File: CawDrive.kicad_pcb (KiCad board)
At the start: 4 copper layers, 60 x 60 mm, 112 parts, among them CN1 XT60PW-M, CN2 MR60PW-M, J1 Conn_01x04_Pin, J2 USB_B_Micro, Q1 IRF7480MTRPBF, Q2 IRF7480MTRPBF, Q3 IRF7480MTRPBF, Q4 IRF7480MTRPBF, Q5 IRF7480MTRPBF, Q6 IRF7480MTRPBF, SW1 B3U-1000P, U1 STM32F446RETx, U2 ISO1044BDR, U3 CH340K, U4 AMS1117-3.3, U5 DRV8323RSRGZR, Y1 16MHz

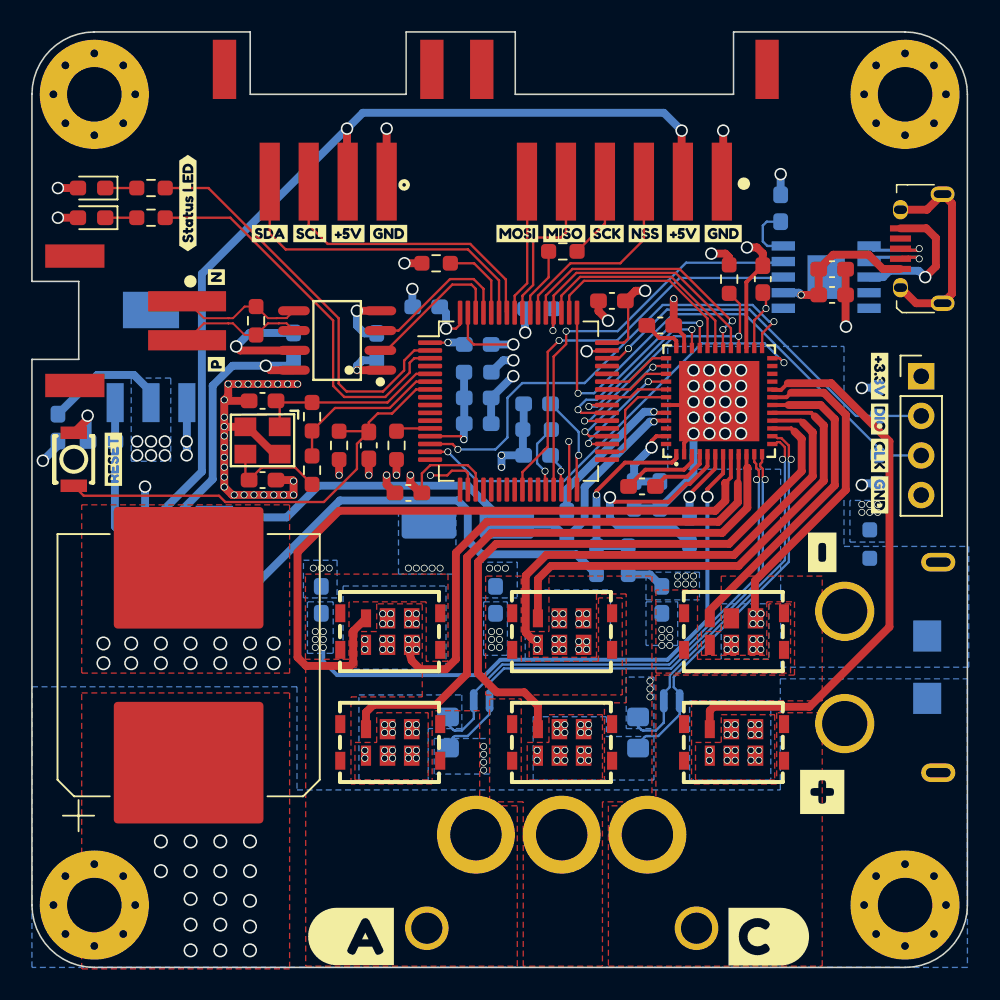
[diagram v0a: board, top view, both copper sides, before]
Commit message: 参考MIT驱动器进行改版
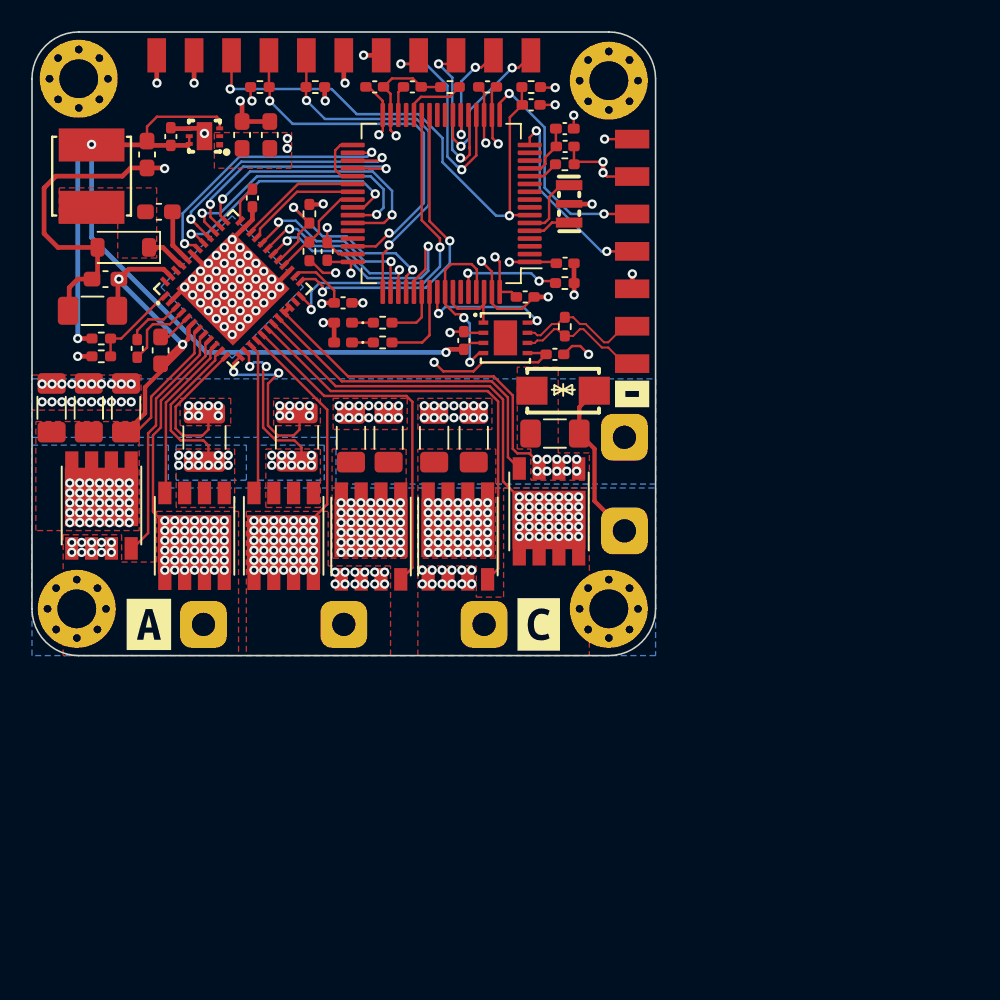
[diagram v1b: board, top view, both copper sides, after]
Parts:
- removed C10: 10uF, Capacitor_SMD:C_0603_1608Metric_Pad1.08x0.95mm_HandSolder
- removed C11, C13: 0.1uF, Capacitor_SMD:C_0603_1608Metric_Pad1.08x0.95mm_HandSolder
- removed C17, C19: 2.2uF/50V, Capacitor_SMD:C_0603_1608Metric_Pad1.08x0.95mm_HandSolder
- removed C18: 470uF/50V, Capacitor_SMD:CP_Elec_16x17.5
- removed CN1: XT60PW-M, Rick_Connector:XT60PW-M
- removed CN2: MR60PW-M, Rick_Connector:MR60PW-M
- removed FPC1: XH-6PWB, Rick_Connector:XH-6PWB
- removed FPC2: XH-4PWB, Rick_Connector:XH-4PWB
- removed FPC3: XH-2PWB, Rick_Connector:XH-2PWB
- removed the G*** at (167.5, 121.0)
- removed J2: USB_B_Micro, Rick_USB:Micro_USB_B_SMD
- removed NT1, NT2, NT3, NT4: NetTie_2, NetTie:NetTie-2_SMD_Pad0.5mm
- removed Q1, Q2, Q3, Q4, Q5, Q6: IRF7480MTRPBF, Rick_MOSFET:IRF7480MTRPBF
- removed R12: 510, Resistor_SMD:R_0603_1608Metric_Pad0.98x0.95mm_HandSolder
- removed R15: 1mΩ, Resistor_SMD:R_0805_2012Metric_Pad1.20x1.40mm_HandSolder
- removed R20: 10k, Resistor_SMD:R_0603_1608Metric_Pad0.98x0.95mm_HandSolder
- removed R4: 0, Resistor_SMD:R_0603_1608Metric_Pad0.98x0.95mm_HandSolder
- removed R7: 33, Resistor_SMD:R_0603_1608Metric_Pad0.98x0.95mm_HandSolder
- removed SW1: B3U-1000P, Rick_Switch:B3U-1000P
- removed U3: CH340K, Rick_Interface_USB:CH340K
- removed U4: AMS1117-3.3, Rick_Regulator_Linear:AMS1117-3.3
- removed Y1: 16MHz, Rick_Device:Crystal_16MHz_GND24
- removed kibuzzard-64D4C305: G***, kibuzzard-64D4C305
- removed kibuzzard-64D4C31F: G***, kibuzzard-64D4C31F
- removed kibuzzard-64D4C332: G***, kibuzzard-64D4C332
- removed kibuzzard-64D4C34A: G***, kibuzzard-64D4C34A
- removed kibuzzard-64D4C405: G***, kibuzzard-64D4C405
- removed kibuzzard-64D4C58A: G***, kibuzzard-64D4C58A
- removed kibuzzard-64D4C598: G***, kibuzzard-64D4C598
- removed kibuzzard-64D4C5A5: G***, kibuzzard-64D4C5A5
- removed kibuzzard-64D4C640: G***, kibuzzard-64D4C640
- removed kibuzzard-64D4C647: G***, kibuzzard-64D4C647
- removed kibuzzard-64D4C6F3: G***, kibuzzard-64D4C6F3
- removed kibuzzard-64D4C6FE: G***, kibuzzard-64D4C6FE
- removed kibuzzard-64D4C824: G***, kibuzzard-64D4C824
- removed kibuzzard-64D4C87F: G***, kibuzzard-64D4C87F
- removed kibuzzard-64D4C8BC: G***, kibuzzard-64D4C8BC
- removed kibuzzard-64D4C8D7: G***, kibuzzard-64D4C8D7
- removed kibuzzard-64D4C8F8: G***, kibuzzard-64D4C8F8
- removed kibuzzard-64D4C907: G***, kibuzzard-64D4C907
- removed kibuzzard-64D4C919: G***, kibuzzard-64D4C919
- removed kibuzzard-64D4C952: G***, kibuzzard-64D4C952
- removed kibuzzard-64D63200: G***, kibuzzard-64D63200
- removed kibuzzard-64D63E68: G***, kibuzzard-64D63E68
- removed kibuzzard-64D641B0: G***, kibuzzard-64D641B0
- removed kibuzzard-64D6424D: G***, kibuzzard-64D6424D
- removed kibuzzard-64D642FB: G***, kibuzzard-64D642FB
- removed kibuzzard-64D648D8: G***, kibuzzard-64D648D8
- removed kibuzzard-64E4B26A: G***, kibuzzard-64E4B26A
- added C31: 1uF, Capacitor_SMD:C_0402_1005Metric_Pad0.74x0.62mm_HandSolder, F.Cu at (134.1, 80.7)
- added C32: 1uF, Capacitor_SMD:C_0402_1005Metric_Pad0.74x0.62mm_HandSolder, F.Cu at (140.0, 87.4)
- added C33: 0.1uF/50V, Capacitor_SMD:C_0603_1608Metric_Pad1.08x0.95mm_HandSolder, F.Cu at (124.7, 85.9)
- added C34: 22uF, Capacitor_SMD:C_0603_1608Metric_Pad1.08x0.95mm_HandSolder, F.Cu at (133.5, 76.6)
- added C35: 22uF, Capacitor_SMD:C_0603_1608Metric_Pad1.08x0.95mm_HandSolder, F.Cu at (135.3, 76.6)
- added H5: MountingHole_Pad, CawDrive_Connector:POWER_PAD, F.Cu at (131.0, 108.0)
- added H6: MountingHole_Pad, CawDrive_Connector:POWER_PAD, F.Cu at (140.0, 108.0)
- added H7: MountingHole_Pad, CawDrive_Connector:POWER_PAD, F.Cu at (149.0, 108.0)
- added H8: MountingHole_Pad, CawDrive_Connector:POWER_PAD, F.Cu at (158.0, 96.0)
- added H9: MountingHole_Pad, CawDrive_Connector:POWER_PAD, F.Cu at (158.0, 102.0)
- added J4: Conn_01x07_Pin, CawDrive_Connector:SOIC-7, F.Cu at (158.5, 84.1)
- added Q10: TPH3R704PL, Rick_MOSFET:TPHR8504PL,L1Q, F.Cu at (136.1, 102.3)
- added Q11: TPH3R704PL, Rick_MOSFET:TPHR8504PL,L1Q, F.Cu at (147.3, 102.4)
- added Q12: TPH3R704PL, Rick_MOSFET:TPHR8504PL,L1Q, F.Cu at (153.2, 100.8)
- added Q7: TPH3R704PL, Rick_MOSFET:TPHR8504PL,L1Q, F.Cu at (124.5, 100.4)
- added Q8: TPH3R704PL, Rick_MOSFET:TPHR8504PL,L1Q, F.Cu at (130.4, 102.3)
- added Q9: TPH3R704PL, Rick_MOSFET:TPHR8504PL,L1Q, F.Cu at (141.8, 102.4)
- added R18: 1mΩ, Resistor_SMD:R_1210_3225Metric_Pad1.30x2.65mm_HandSolder, F.Cu at (131.1, 96.0)
- added U6: XC6220B331ER-G, Rick_Regulator_Linear:XC6220B331ER-G_USP-6C_L2.0-W1.8-P0.50-BL-EP, F.Cu at (131.1, 76.7)
- added X1: Crystal_16MHz_15pF_3P, Rick_Crystal:Crystal_SMD3213-3P, F.Cu at (154.5, 81.0)
- added kibuzzard-65071042: G***, kibuzzard-65071042, B.Cu at (140.0, 81.5)
- added kibuzzard-6507110A: G***, kibuzzard-6507110A, B.Cu at (154.0, 79.5)
- added kibuzzard-650712D1: G***, kibuzzard-650712D1, B.Cu at (122.0, 83.5)
- added kibuzzard-650713F8: G***, kibuzzard-650713F8, B.Cu at (139.7, 73.0)
- added kibuzzard-65071EE4: G***, kibuzzard-65071EE4, B.Cu at (130.0, 78.0)
- added kibuzzard-65072293: G***, kibuzzard-65072293, F.Cu at (127.5, 108.0)
- added kibuzzard-650722BD: G***, kibuzzard-650722BD, F.Cu at (152.5, 108.0)
- added kibuzzard-650722D4: G***, kibuzzard-650722D4, F.Cu at (158.5, 93.2)
- C1, C12, C2, C4, C6, C9: footprint Capacitor_SMD:C_0603_1608Metric_Pad1.08x0.95mm_HandSolder -> Capacitor_SMD:C_0402_1005Metric_Pad0.74x0.62mm_HandSolder; moved to F.Cu
- C14: value 12pF -> 0.1uF; footprint Capacitor_SMD:C_0603_1608Metric_Pad1.08x0.95mm_HandSolder -> Capacitor_SMD:C_0402_1005Metric_Pad0.74x0.62mm_HandSolder
- C15: value 0.1uF -> 0.1uF/50V
- C16: value 12pF -> 22uF
- C20: value 100nF/50V -> 10uF/50V; footprint Capacitor_SMD:C_0603_1608Metric_Pad1.08x0.95mm_HandSolder -> Capacitor_SMD:C_1206_3216Metric_Pad1.33x1.80mm_HandSolder; moved to F.Cu
- C21: value 10uF -> 10uF/50V; footprint Capacitor_SMD:C_0603_1608Metric_Pad1.08x0.95mm_HandSolder -> Capacitor_SMD:C_1206_3216Metric_Pad1.33x1.80mm_HandSolder; moved to F.Cu
- C22: value 2.2uF/50V -> 10uF/50V; footprint Capacitor_SMD:C_0603_1608Metric_Pad1.08x0.95mm_HandSolder -> Capacitor_SMD:C_1206_3216Metric_Pad1.33x1.80mm_HandSolder; moved to F.Cu
- C23: value 0.1uF -> 10uF/50V; footprint Capacitor_SMD:C_0603_1608Metric_Pad1.08x0.95mm_HandSolder -> Capacitor_SMD:C_1206_3216Metric_Pad1.33x1.80mm_HandSolder; moved to F.Cu
- C24: value 4.7uF -> 10uF/50V; footprint Capacitor_SMD:C_0603_1608Metric_Pad1.08x0.95mm_HandSolder -> Capacitor_SMD:C_1206_3216Metric_Pad1.33x1.80mm_HandSolder; moved to F.Cu
- C25: value 47nF/50v -> 10uF/50V; footprint Capacitor_SMD:C_0603_1608Metric_Pad1.08x0.95mm_HandSolder -> Capacitor_SMD:C_1206_3216Metric_Pad1.33x1.80mm_HandSolder
- C26: value 1uF/50v -> 10uF/50V; footprint Capacitor_SMD:C_0603_1608Metric_Pad1.08x0.95mm_HandSolder -> Capacitor_SMD:C_1206_3216Metric_Pad1.33x1.80mm_HandSolder; moved to F.Cu
- C27: value 10uF/50v -> 47nF/50V; footprint Capacitor_SMD:C_0603_1608Metric_Pad1.08x0.95mm_HandSolder -> Capacitor_SMD:C_0402_1005Metric_Pad0.74x0.62mm_HandSolder; moved to F.Cu
- C28: value 1uF -> 1uF/50V
- C29: value 1uF -> 10uF/50V; footprint Capacitor_SMD:C_0603_1608Metric_Pad1.08x0.95mm_HandSolder -> Capacitor_SMD:C_1206_3216Metric_Pad1.33x1.80mm_HandSolder
- C3, C5: footprint Capacitor_SMD:C_0603_1608Metric_Pad1.08x0.95mm_HandSolder -> Capacitor_SMD:C_0402_1005Metric_Pad0.74x0.62mm_HandSolder
- C30: value 1uF/50v -> 0.1uF/50V; footprint Capacitor_SMD:C_0603_1608Metric_Pad1.08x0.95mm_HandSolder -> Capacitor_SMD:C_1206_3216Metric_Pad1.33x1.80mm_HandSolder; moved to F.Cu
- C7: value 10uF -> 1uF; footprint Capacitor_SMD:C_0603_1608Metric_Pad1.08x0.95mm_HandSolder -> Capacitor_SMD:C_0402_1005Metric_Pad0.74x0.62mm_HandSolder; moved to F.Cu
- C8: value 100nF -> 0.1uF; footprint Capacitor_SMD:C_0603_1608Metric_Pad1.08x0.95mm_HandSolder -> Capacitor_SMD:C_0402_1005Metric_Pad0.74x0.62mm_HandSolder; moved to F.Cu
- D1: footprint LED_SMD:LED_0603_1608Metric_Pad1.05x0.95mm_HandSolder -> LED_SMD:LED_0402_1005Metric_Pad0.77x0.64mm_HandSolder
- D2: value DRV_A_STA_LED -> DRV_STA_LED; footprint LED_SMD:LED_0603_1608Metric_Pad1.05x0.95mm_HandSolder -> LED_SMD:LED_0402_1005Metric_Pad0.77x0.64mm_HandSolder
- D3: footprint Diode_SMD:D_SMA_Handsoldering -> Diode_SMD:D_SOD-123; moved to F.Cu
- H1, H2, H3, H4: footprint MountingHole:MountingHole_3.5mm_Pad_Via -> MountingHole:MountingHole_2.5mm_Pad_Via
- J1: value Conn_01x04_Pin -> Conn_01x11_Pin; footprint Connector_PinHeader_2.54mm:PinHeader_1x04_P2.54mm_Vertical -> CawDrive_Connector:SOIC-11
- L1: footprint Inductor_SMD:L_0603_1608Metric_Pad1.05x0.95mm_HandSolder -> Inductor_SMD:L_0402_1005Metric_Pad0.77x0.64mm_HandSolder; moved to F.Cu
- L2: value 22uH -> 22uH_±20%_1.4A; footprint Inductor_SMD:L_6.3x6.3_H3 -> Rick_Inductor:LQH5BPB220MT0L_IND-SMD_L5.0-W5.0; moved to F.Cu
- R1, R2, R8, R9: footprint Resistor_SMD:R_0603_1608Metric_Pad0.98x0.95mm_HandSolder -> Resistor_SMD:R_0402_1005Metric_Pad0.72x0.64mm_HandSolder
- R10: value 1M -> 10k; footprint Resistor_SMD:R_0603_1608Metric_Pad0.98x0.95mm_HandSolder -> Resistor_SMD:R_0402_1005Metric_Pad0.72x0.64mm_HandSolder
- R11: value 10k -> 510; footprint Resistor_SMD:R_0603_1608Metric_Pad0.98x0.95mm_HandSolder -> Resistor_SMD:R_0402_1005Metric_Pad0.72x0.64mm_HandSolder
- R13: value 47 -> 54.9k; footprint Resistor_SMD:R_0603_1608Metric_Pad0.98x0.95mm_HandSolder -> Resistor_SMD:R_0402_1005Metric_Pad0.72x0.64mm_HandSolder
- R14: value 1mΩ -> 10k; footprint Resistor_SMD:R_0805_2012Metric_Pad1.20x1.40mm_HandSolder -> Resistor_SMD:R_0402_1005Metric_Pad0.72x0.64mm_HandSolder; moved to F.Cu
- R16: value 54.9k -> 10k; footprint Resistor_SMD:R_0603_1608Metric_Pad0.98x0.95mm_HandSolder -> Resistor_SMD:R_0402_1005Metric_Pad0.72x0.64mm_HandSolder; moved to F.Cu
- R17, R3, R5, R6: footprint Resistor_SMD:R_0603_1608Metric_Pad0.98x0.95mm_HandSolder -> Resistor_SMD:R_0402_1005Metric_Pad0.72x0.64mm_HandSolder; moved to F.Cu
- R19: value 10k -> 1mΩ; footprint Resistor_SMD:R_0603_1608Metric_Pad0.98x0.95mm_HandSolder -> Resistor_SMD:R_1210_3225Metric_Pad1.30x2.65mm_HandSolder; moved to F.Cu
- TV1: footprint Rick_Diode:SMAJ36CA_TR13 -> Rick_Diode:SMAJ36CA_TR13_SMA(DO-214AC); moved to F.Cu
- U2: value ISO1044BDR -> NCV7342MW3R2G; footprint Rick_CAN:ISO1044BDR -> Rick_CAN:NCV7342MW3R2G_DFN-8_L3.0-W3.0-P0.65-BL-EP
- U5: footprint Rick_Drive:DRV8323RSRGZR -> Rick_Drive:DRV8323RS_QFN-48-EP(7x7)
- moved R5 44.5 mm to (134.6, 73.5), turned to 180 degrees
- moved R6 43.6 mm to (138.2, 73.5), turned to 0 degrees
- moved J1 42.4 mm to (140.0, 71.5)
- moved C22 41.0 mm to (121.3, 94.1)
- moved G*** 39.0 mm to (154.0, 86.0)
- moved C30 38.3 mm to (123.9, 87.9), turned to 180 degrees
- moved C27 33.2 mm to (126.8, 90.3)
- moved R14 32.8 mm to (124.4, 90.8), turned to 180 degrees
- moved C28 32.1 mm to (128.2, 90.4), turned to 90 degrees
- moved U5 32.0 mm to (132.9, 86.5), turned to 45 degrees
- moved TV1 29.3 mm to (154.1, 93.0), turned to 180 degrees
- moved C20 29.2 mm to (126.0, 94.1), turned to 90 degrees
- moved R16 28.9 mm to (137.8, 81.7), turned to -90 degrees
- moved R17 28.5 mm to (137.8, 84.1), turned to 90 degrees
- moved D3 28.4 mm to (125.9, 83.8)
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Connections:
- C12 pad 1: +5V -> GND
- C12 pad 2: GND -> +5V
- C14 pad 1: /HSE_IN -> /RESET
- C15 pad 1: /RESET -> /DRV8323RSRGZR/CB
- C15 pad 2: GND -> /DRV8323RSRGZR/SW
- C16 pad 1: Net-(C16-Pad1) -> +5V
- C20 pad 1: /DRV8323RSRGZR/CB -> +36V
- C20 pad 2: /DRV8323RSRGZR/SW -> GND
- C21 pad 1: +5V -> +36V
- C22 pad 2: GND1 -> GND
- C23 pad 1: +5V -> +36V
- C24 pad 1: +3.3V -> +36V
- C25 pad 1: Net-(U5-CPL) -> +36V
- C25 pad 2: Net-(U5-CPH) -> GND
- C26 pad 2: Net-(U5-VCP) -> GND
- C27 pad 1: +36V -> Net-(U5-CPL)
- C27 pad 2: GND1 -> Net-(U5-CPH)
- C28 pad 1: Net-(U5-DVDD) -> +36V
- C28 pad 2: GND -> Net-(U5-VCP)
- C29 pad 1: +3.3V -> +36V
- C30 pad 2: GND1 -> GND
- C7 pad 1: +3.3VA -> +5V
- D3 pad 2: GND1 -> GND
- H1 pad 1: GND -> unconnected-(H1-Pad1)
- H2 pad 1: GND -> unconnected-(H2-Pad1)
- H3 pad 1: GND1 -> unconnected-(H3-Pad1)
- H4 pad 1: GND1 -> unconnected-(H4-Pad1)
- J1 pad 2: /SWDIO -> GND
- J1 pad 3: /SWCLK -> /RESET
- J1 pad 4: GND -> /SWDIO
- R10 pad 1: /HSE_IN -> +3.3V
- R10 pad 2: /HSE_OUT -> /RESET
- R11 pad 1: +3.3V -> Net-(D2-K)
- R11 pad 2: /RESET -> /DRV_STA
- R13 pad 1: /HSE_OUT -> +5V
- R13 pad 2: Net-(C16-Pad1) -> /DRV8323RSRGZR/FB
- R14 pad 1: Net-(NT1-Pad1) -> /DRV8323RSRGZR/FB
- R14 pad 2: GND1 -> GND
- R16 pad 1: +5V -> +3.3V
- R16 pad 2: /DRV8323RSRGZR/FB -> /SPI3_MISO
- R17 pad 1: /DRV8323RSRGZR/FB -> +3.3V
- R17 pad 2: GND1 -> /DRV_FAULT
- R19 pad 1: +3.3V -> /DRV8323RSRGZR/SPB
- R19 pad 2: /SPI3_MISO -> GND
- R5 pad 1: +3.3V -> /SWDIO
- R5 pad 2: /SWDIO -> +3.3V
- TV1 pad 2: GND1 -> GND
- U1 pad 14: /ADC1_IN0 -> unconnected-(U1-PA0-Pad14)
- U1 pad 15: /ADC1_IN1 -> unconnected-(U1-PA1-Pad15)
- U1 pad 16: unconnected-(U1-PA2-Pad16) -> /USART2_TX
- U1 pad 17: unconnected-(U1-PA3-Pad17) -> /USART2_RX
- U1 pad 2: /MCU_STA -> unconnected-(U1-PC13-Pad2)
- U1 pad 20: unconnected-(U1-PA4-Pad20) -> /SPI1_NSS
- U1 pad 21: unconnected-(U1-PA5-Pad21) -> /SPI1_SCK
- U1 pad 22: unconnected-(U1-PA6-Pad22) -> /SPI1_MISO
- U1 pad 23: unconnected-(U1-PA7-Pad23) -> /SPI1_MOSI
- U1 pad 25: /CH340_TXD -> unconnected-(U1-PC5-Pad25)
- U1 pad 26: unconnected-(U1-PB0-Pad26) -> /ADC1_IN8
- U1 pad 27: unconnected-(U1-PB1-Pad27) -> /ADC1_IN9
- U1 pad 29: /CH340_RXD -> unconnected-(U1-PB10-Pad29)
- U1 pad 3: /DRV_A_STA -> unconnected-(U1-PC14-Pad3)
- U1 pad 33: unconnected-(U1-PB12-Pad33) -> /TIM1_BKIN
- U1 pad 37: unconnected-(U1-PC6-Pad37) -> /TIM1_BKIN
- U1 pad 38: /DRV_FAULT -> /DRV_CAL
- U1 pad 40: /DRV_CAL -> /DRV_FAULT
- U1 pad 54: /SPI1_NSS -> /MCU_STA
- U1 pad 55: /SPI1_SCK -> /DRV_STA
- U1 pad 56: /SPI1_MISO -> /CAN_STB
- U1 pad 57: /SPI1_MOSI -> /CAN_RX
- U1 pad 58: /I2C1_SCL -> /CAN_TX
- U1 pad 59: /I2C1_SDA -> unconnected-(U1-PB7-Pad59)
- U1 pad 61: /CAN1_RX -> /CAN_RX
- U1 pad 62: /CAN1_TX -> /CAN_TX
- U2 pad 1: +3.3V -> /CAN_TX
- U2 pad 2: /CAN1_TX -> GND
- U2 pad 3: /CAN1_RX -> +5V
- U2 pad 4: GND -> /CAN_RX
- U2 pad 5: /CAN_N -> +3.3V
- U2 pad 6: /CAN_P -> /CAN_N
- U2 pad 7: GND -> /CAN_P
- U2 pad 8: +5V -> /CAN_STB
- U5 pad 11: /DRV8323RSRGZR/SNSA_P -> /DRV8323RSRGZR/SPA
- U5 pad 12: /DRV8323RSRGZR/SNSA_N -> GND
- U5 pad 13: /DRV8323RSRGZR/SNSB_N -> GND
- U5 pad 14: /DRV8323RSRGZR/SNSB_P -> /DRV8323RSRGZR/SPB
- U5 pad 2: GND1 -> GND
- U5 pad 21: unconnected-(U5-SPC-Pad21) -> GND
- U5 pad 22: unconnected-(U5-SNC-Pad22) -> GND
- U5 pad 24: /ADC1_IN1 -> /ADC1_IN9
- U5 pad 25: /ADC1_IN0 -> /ADC1_IN8
- U5 pad 43: GND1 -> GND
- U5 pad 49: GND1 -> GND
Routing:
- net +5V: track 129.1 -> 61.7 mm
- net /DRV8323RSRGZR/SW: track 35.6 -> 2.56 mm, vias 1 -> 0
- net /DRV8323RSRGZR/GLB: track 40.8 -> 9.74 mm
- net /DRV8323RSRGZR/GHA: track 45.8 -> 15.7 mm
- net /ADC1_IN0: track 30.0 -> 0.00 mm, vias 2 -> 0
- net /DRV8323RSRGZR/SNSA_P: track 29.4 -> 0.00 mm, vias 1 -> 0
- net /DRV8323RSRGZR/SNSA_N: track 29.1 -> 0.00 mm, vias 1 -> 0
- net /ADC1_IN1: track 28.5 -> 0.00 mm, vias 2 -> 0
- net /DRV8323RSRGZR/GLA: track 38.8 -> 10.8 mm
- net /CH340_TXD: track 26.6 -> 0.00 mm, vias 1 -> 0
- net /CH340_RXD: track 26.3 -> 0.00 mm, vias 1 -> 0
- net /DRV_A_STA: track 25.6 -> 0.00 mm
- net /MCU_STA: track 26.3 -> 3.68 mm
- net /ADC1_IN9: track 0.00 -> 21.5 mm, vias 0 -> 2
- net /I2C1_SDA: track 21.3 -> 0.00 mm
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- added copper zone on F.Cu, net +3.3V
- added copper zone on In1.Cu, net +3.3V
- added copper zone on In1.Cu, net /DRV8323RSRGZR/PHASA
- added copper zone on In1.Cu, net /DRV8323RSRGZR/PHASB
- added copper zone on In1.Cu, net /DRV8323RSRGZR/PHASC
- added copper zone on B.Cu, net /DRV8323RSRGZR/SPA
- added copper zone on F.Cu, net /DRV8323RSRGZR/SPA
- added copper zone on B.Cu, net /DRV8323RSRGZR/SPB
- added copper zone on F.Cu, net /DRV8323RSRGZR/SPB
- added copper zone on F.Cu, net /DRV8323RSRGZR/SW
- added copper zone on F.Cu, net GND
- added copper zone on In2.Cu, net GND
- removed copper zone on B.Cu, net +3.3V
- removed copper zone on In2.Cu, net +3.3V
- removed copper zone on B.Cu, net /DRV8323RSRGZR/PHASA
- removed copper zone on B.Cu, net /DRV8323RSRGZR/PHASB
- removed copper zone on B.Cu, net /DRV8323RSRGZR/PHASC
- removed copper zone on B.Cu, net GND1
- removed copper zone on F.Cu, net GND1
- removed copper zone on In1.Cu, net GND1
- removed copper zone on B.Cu, net Net-(NT1-Pad1)
- removed copper zone on F.Cu, net Net-(NT1-Pad1)
- removed copper zone on B.Cu, net Net-(NT3-Pad1)
- removed copper zone on F.Cu, net Net-(NT3-Pad1)
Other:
- board size 60 x 60 mm -> 40 x 40 mm

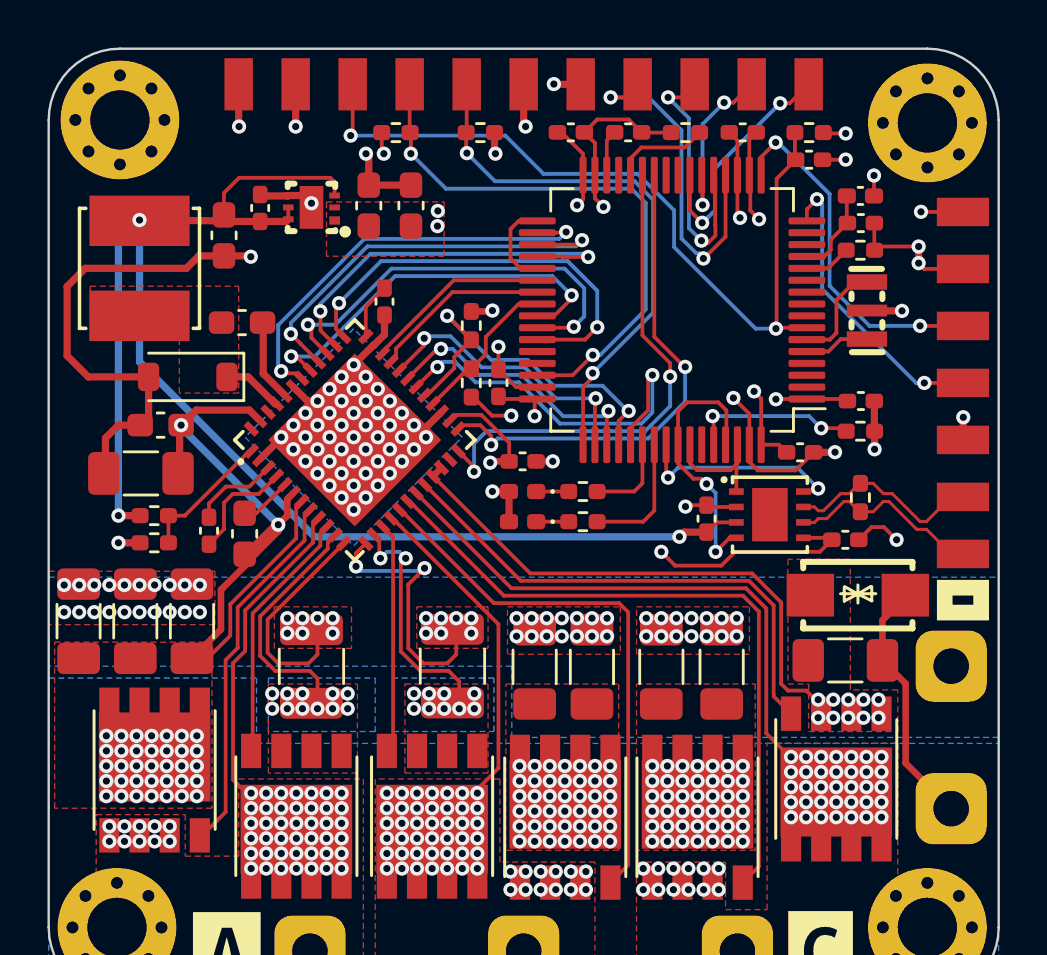
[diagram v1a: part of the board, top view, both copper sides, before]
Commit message: 将线性稳压芯片和CAN芯片替换成TI的相关型号
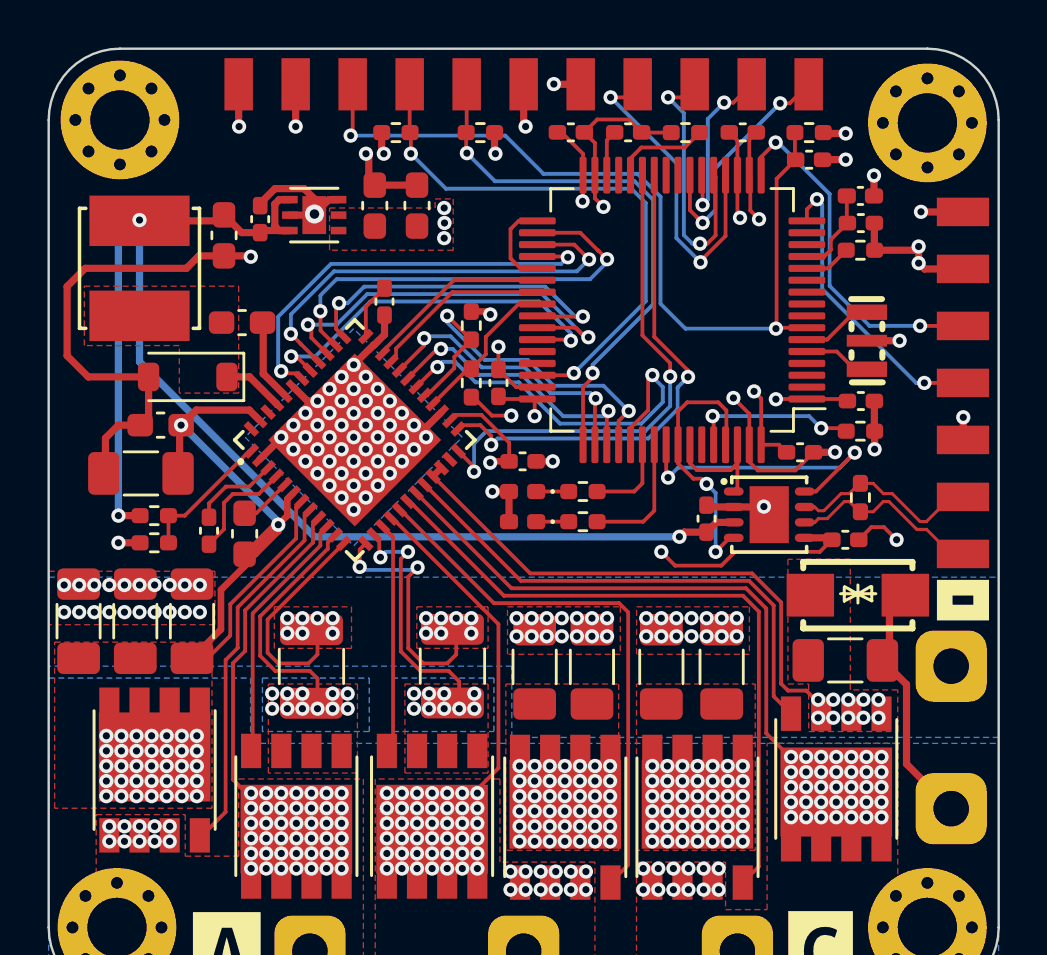
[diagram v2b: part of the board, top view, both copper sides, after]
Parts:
- removed U6: XC6220B331ER-G, Rick_Regulator_Linear:XC6220B331ER-G_USP-6C_L2.0-W1.8-P0.50-BL-EP
- added U3: TCAN1044DRBRQ1, Rick_CAN:TCAN1044DRBRQ1_DFN-8_L3.0-W3.0-P0.65-TL-EP2.4, F.Cu at (150.3, 89.6)
- U2: value NCV7342MW3R2G -> TLV76733DRVR; footprint Rick_CAN:NCV7342MW3R2G_DFN-8_L3.0-W3.0-P0.65-BL-EP -> Rick_Regulator_Linear:TLV76733DRVR_SON65P200X200X80-7N
- moved U2 23.0 mm to (131.2, 77.0), turned to 180 degrees
- moved X1 1.27 mm to (154.5, 82.3)
- moved C7 0.47 mm to (128.9, 77.2)
- moved C34 0.25 mm to (133.7, 76.6)
- moved C35 0.25 mm to (135.5, 76.6)
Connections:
- U2 pad 1: /CAN_TX -> +3.3V
- U2 pad 2: GND -> +3.3V
- U2 pad 3: +5V -> GND
- U2 pad 4: /CAN_RX -> +5V
- U2 pad 5: +3.3V -> GND
- U2 pad 6: /CAN_N -> +5V
- U2 pad 7: /CAN_P -> GND
- U5 pad 37: /TIM1_PWM_CH3 -> /TIM1_PWM_CH1
- U5 pad 38: /TIM1_PWM_CH3N -> /TIM1_PWM_CH1N
- U5 pad 41: /TIM1_PWM_CH1 -> /TIM1_PWM_CH3
- U5 pad 42: /TIM1_PWM_CH1N -> /TIM1_PWM_CH3N
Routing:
- net +5V: track 61.7 -> 57.2 mm
- net /CAN_STB: track 8.95 -> 12.5 mm
- net GND: track 122.5 -> 125.8 mm
- net /TIM1_PWM_CH3: track 18.0 -> 16.1 mm
- net /TIM1_PWM_CH1: track 16.5 -> 14.6 mm
- net /RESET: track 34.3 -> 36.0 mm
- net /TIM1_PWM_CH3N: track 16.4 -> 17.9 mm
- net /HSE_OUT: track 4.34 -> 3.01 mm
- net /TIM1_PWM_CH2: track 17.9 -> 16.9 mm
- net /CAN_TX: track 5.01 -> 5.83 mm
- net /SPI1_NSS: track 14.8 -> 14.0 mm
- net /TIM1_PWM_CH2N: track 17.8 -> 18.4 mm
- net /TIM1_PWM_CH1N: track 18.0 -> 18.5 mm
- net +3.3V: track 43.4 -> 43.0 mm, vias 18 -> 19
